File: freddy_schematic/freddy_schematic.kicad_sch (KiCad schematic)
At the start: 2 parts, among them U1 ESP32-C3-DevKitC-02

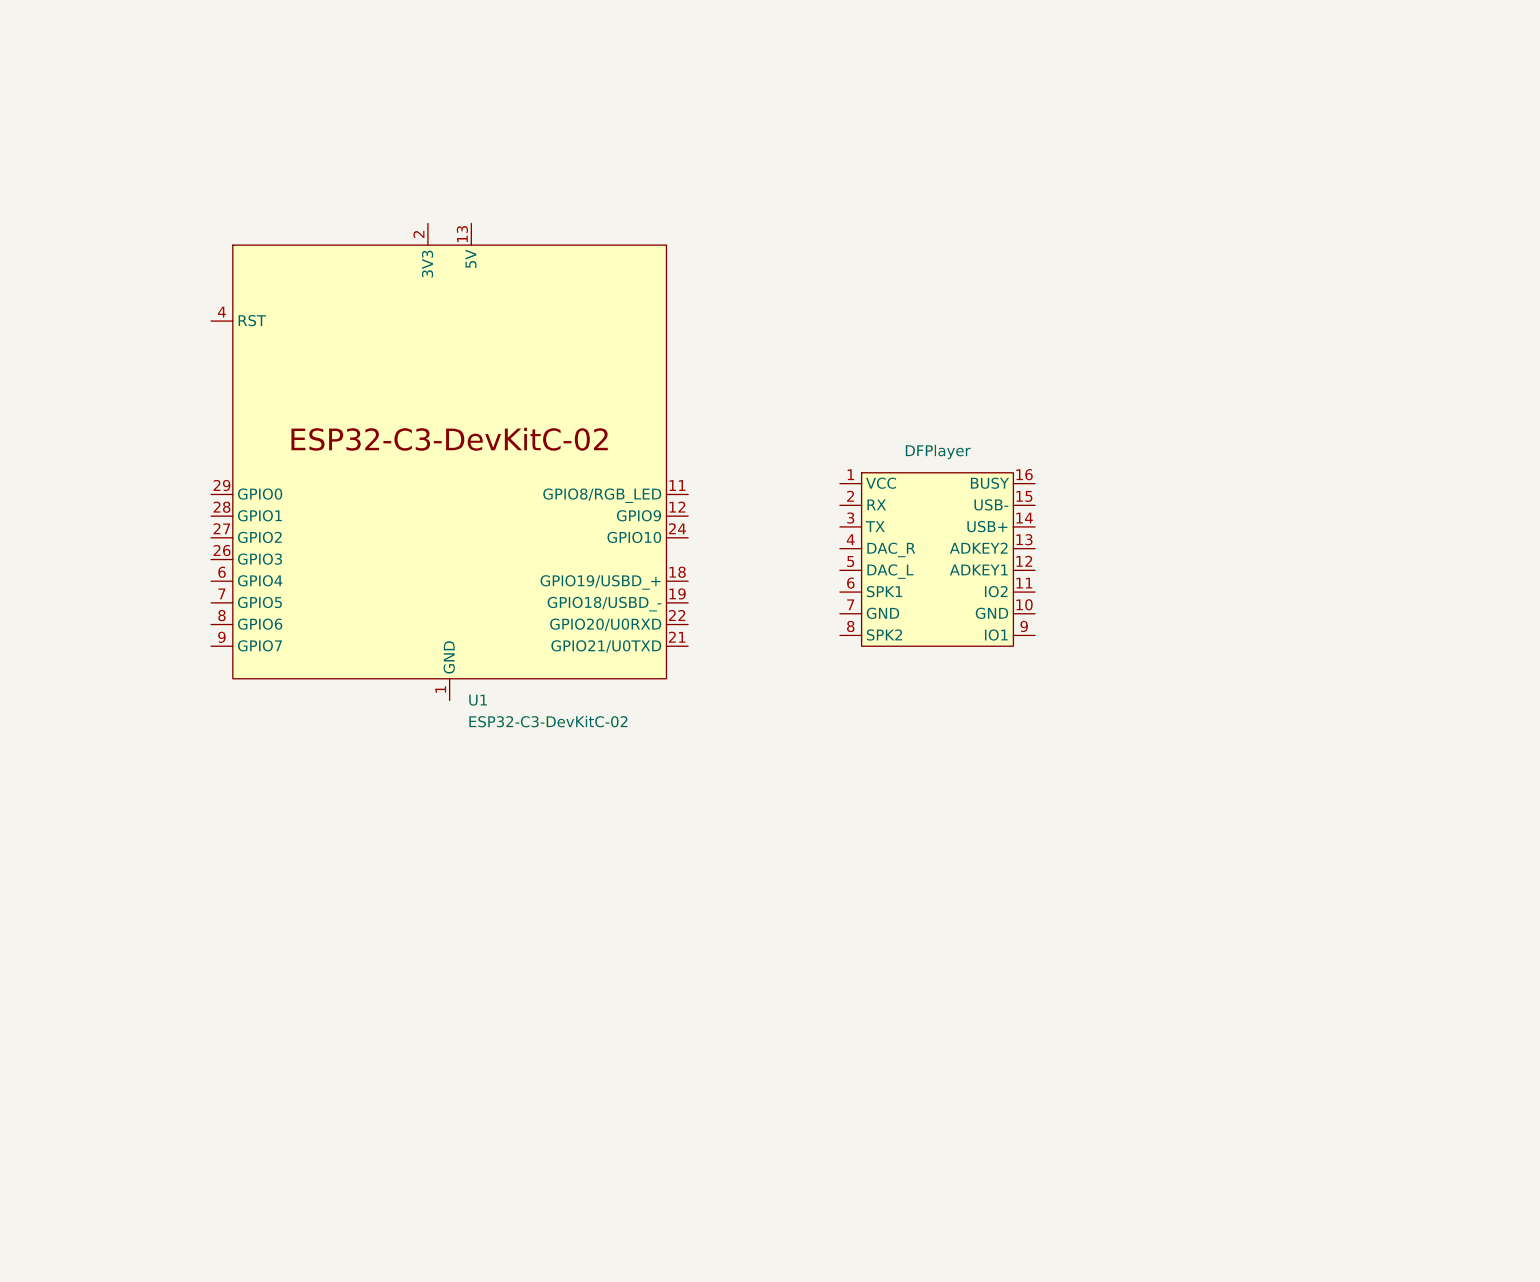
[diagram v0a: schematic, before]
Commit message: complete schematic
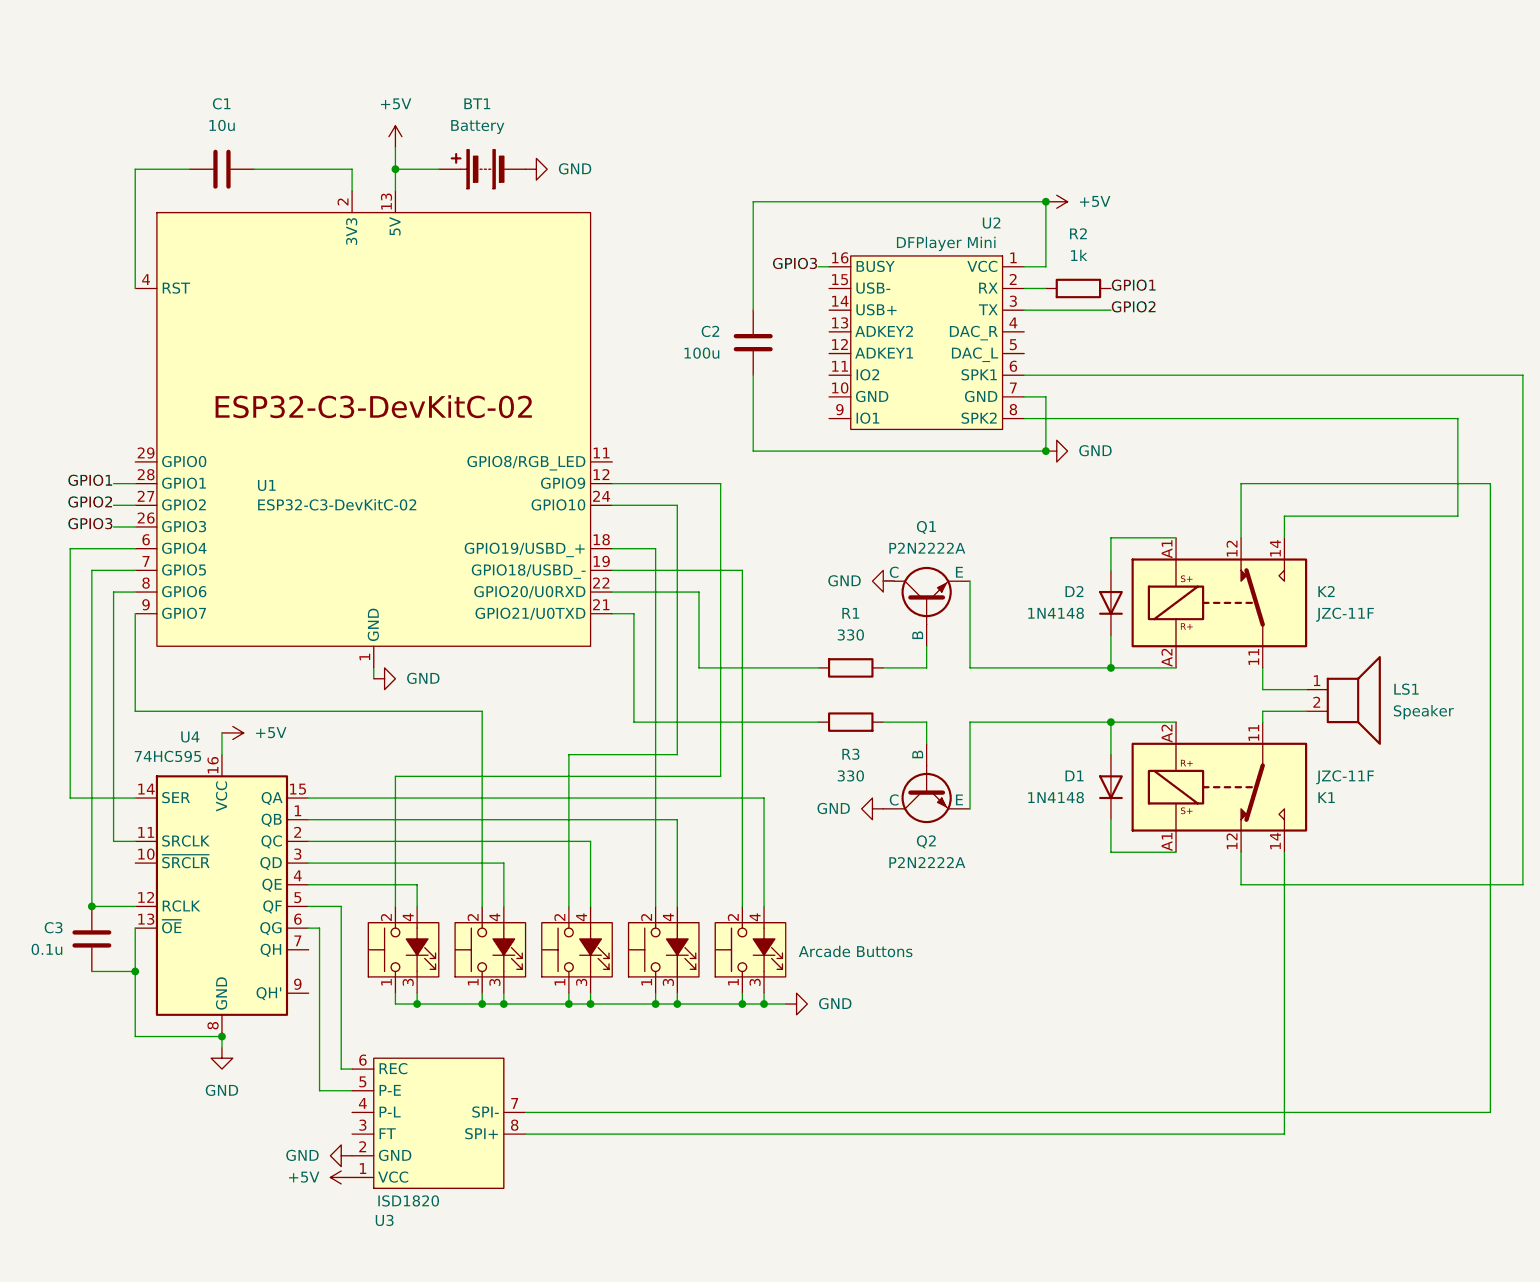
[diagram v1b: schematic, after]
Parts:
- removed DFPlayer: (no value), symbol PCB_periperals:DFPlayer_Mini
- added BT1: Battery, symbol Device:Battery
- added C1: 10u, symbol Device:C
- added C2: 100u, symbol Device:C
- added C3: 0.1u, symbol Device:C
- added D1, D2: 1N4148, Diode_THT:D_DO-35_SOD27_P7.62mm_Horizontal, symbol Diode:1N4148
- added K1, K2: JZC-11F, symbol Relay:Relay_SPDT_Latching_1coil
- added LS1: Speaker, symbol Device:Speaker
- added Q1, Q2: P2N2222A, symbol Simulation_SPICE:NPN
- added R1, R3: 330, symbol Device:R
- added R2: 1k, symbol Device:R
- added SW1: Arcade Buttons, symbol Switch:SW_Push_LED
- added SW2, SW3, SW4, SW5: Arcade Button, symbol Switch:SW_Push_LED
- added U2: DFPlayer Mini, symbol PCB_periperals:DFPlayer_Mini
- added U3: ISD1820, symbol PCB_periperals:ISD1820
- added U4: 74HC595, symbol 74xx:74HC595
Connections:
- net 3V3: now also C1.2
- net GND: now reaches U1.1 (GND), U1.10 (GND), U1.15 (GND), U1.16 (GND), U1.17 (GND), U1.20 (GND), U1.23 (GND), U1.25 (GND), U1.30 (GND), U1.5 (GND)
- net GND: now also BT1.2 (-), C2.2, C3.1, Q1.1 (C), Q2.1 (C), SW1.1, SW1.3 (K), SW2.1, SW2.3 (K), SW3.1, SW3.3 (K), SW4.1, SW4.3 (K), SW5.1, SW5.3 (K), U2.7 (GND), U3.2 (GND), U4.13 (~{OE}), U4.8 (GND)
- net at U1.12 (GPIO9): now also SW1.2
- net at U1.18 (GPIO19/USBD_+): now also SW4.2
- net at U1.19 (GPIO18/USBD_-): now also SW5.2
- net at U1.21 (GPIO21/U0TXD): now also R3.1
- net at U1.22 (GPIO20/U0RXD): now also R1.2
- net at U1.24 (GPIO10): now also SW3.2
- net GPIO3: now reaches U1.26 (GPIO3)
- net GPIO3: now also U2.16 (BUSY)
- net GPIO2: now reaches U1.27 (GPIO2)
- net GPIO2: now also U2.3 (TX)
- net GPIO1: now reaches U1.28 (GPIO1)
- net GPIO1: now also R2.1
- net at U1.4 (RST): now also C1.1
- net at U1.6 (GPIO4): now also U4.14 (SER)
- net at U1.7 (GPIO5): now also C3.2, U4.12 (RCLK)
- net at U1.8 (GPIO6): now also U4.11 (SRCLK)
- net at U1.9 (GPIO7): now also SW2.2
- net 5V renamed +5V
- net +5V: now also BT1.1 (+), C2.1, U2.1 (VCC), U3.1 (VCC), U4.16 (VCC)
- new net: R2.2, U2.2 (RX)
- new net: K1.12, U2.6 (SPK1)
- new net: K2.14, U2.8 (SPK2)
- new net: Q2.2 (B), R3.2
- new net: D1.2 (A), K1.A2, Q2.3 (E)
- new net: K2.11, LS1.1
- new net: K2.12, U3.7 (SPI-)
- new net: D2.2 (A), K2.A1
- new net: D2.1 (K), K2.A2, Q1.3 (E)
- new net: SW1.4 (A), U4.4 (QE)
- new net: K1.11, LS1.2
- new net: D1.1 (K), K1.A1
- new net: U3.5 (P-E), U4.6 (QG)
- new net: U3.6 (REC), U4.5 (QF)
- new net: K1.14, U3.8 (SPI+)
- new net: SW4.4 (A), U4.1 (QB)
- new net: SW2.4 (A), U4.3 (QD)
- new net: SW5.4 (A), U4.15 (QA)
- new net: SW3.4 (A), U4.2 (QC)
- new net: Q1.2 (B), R1.1

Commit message: fixed schematic
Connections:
- net +5V: now also U4.10 (~{SRCLR})
- net 3V3: no longer C1.2
- net GND: now also C1.1
- net at U1.4 (RST): now also C1.2; no longer C1.1
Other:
- moved on the sheet: C1
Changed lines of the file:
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@@
 	(wire
 		(pts
-			(xy 128.27 105.41) (xy 115.57 105.41)
+			(xy 57.15 53.34) (xy 57.15 50.8)
 		)
 		(stroke
@@
 	(wire
 		(pts
-			(xy 125.73 133.35) (xy 125.73 134.62)
+			(xy 128.27 105.41) (xy 115.57 105.41)
 		)
 		(stroke
@@
 	(wire
 		(pts
-			(xy 85.09 120.65) (xy 97.79 120.65)
+			(xy 125.73 133.35) (xy 125.73 134.62)
 		)
 		(stroke
@@
 	(wire
 		(pts
-			(xy 97.79 134.62) (xy 105.41 134.62)
+			(xy 85.09 120.65) (xy 97.79 120.65)
 		)
 		(stroke
@@
 	(wire
 		(pts
-			(xy 138.43 110.49) (xy 138.43 123.19)
+			(xy 97.79 134.62) (xy 105.41 134.62)
 		)
 		(stroke
@@
 	(wire
 		(pts
-			(xy 74.93 138.43) (xy 64.77 138.43)
+			(xy 138.43 110.49) (xy 138.43 123.19)
 		)
 		(stroke
@@
 	(wire
 		(pts
-			(xy 57.15 81.28) (xy 57.15 110.49)
+			(xy 74.93 138.43) (xy 64.77 138.43)
 		)
 		(stroke
@@
 	(wire
 		(pts
-			(xy 71.12 36.83) (xy 64.77 36.83)
+			(xy 57.15 81.28) (xy 57.15 110.49)
 		)
 		(stroke
@@
 	(wire
 		(pts
-			(xy 78.74 36.83) (xy 90.17 36.83)
-		)
-		(stroke
-			(width 0)
-			(type default)
-		)
-	)
-	(wire
-		(pts
 			(xy 179.07 101.6) (xy 179.07 105.41)
 		)
@@
 	(wire
 		(pts
-			(xy 90.17 36.83) (xy 90.17 39.37)
-		)
-		(stroke
-			(width 0)
-			(type default)
-		)
-	)
-	(wire
-		(pts
 			(xy 120.65 86.36) (xy 130.81 86.36)
 		)
@@
 	(wire
 		(pts
-			(xy 64.77 36.83) (xy 64.77 50.8)
-		)
-		(stroke
-			(width 0)
-			(type default)
-		)
-	)
-	(wire
-		(pts
 			(xy 88.9 142.24) (xy 88.9 123.19)
 		)
@@
 	(symbol
 		(lib_id "Device:C")
-		(at 74.93 36.83 90)
+		(at 60.96 50.8 90)
 		(unit 1)
 		(body_style 1)
@@
 		(fields_autoplaced yes)
 		(property "Reference" "C1"
-			(at 74.93 29.21 90)
+			(at 60.96 43.18 90)
 			(show_name no)
 			(do_not_autoplace no)
@@
 		)
 		(property "Value" "10u"
-			(at 74.93 31.75 90)
+			(at 60.96 45.72 90)
 			(show_name no)
 			(do_not_autoplace no)
@@
 		)
 		(property "Footprint" ""
-			(at 78.74 35.8648 0)
+			(at 64.77 49.8348 0)
 			(hide yes)
 			(show_name no)
@@
 		)
 		(property "Datasheet" ""
-			(at 74.93 36.83 0)
+			(at 60.96 50.8 0)
 			(hide yes)
 			(show_name no)
@@
 		)
 		(property "Description" "Unpolarized capacitor"
-			(at 74.93 36.83 0)
+			(at 60.96 50.8 0)
 			(hide yes)
 			(show_name no)
@@
 	(symbol
 		(lib_id "power:GND")
+		(at 57.15 53.34 0)
+		(unit 1)
+		(body_style 1)
+		(exclude_from_sim no)
+		(in_bom yes)
+		(on_board yes)
+		(in_pos_files yes)
+		(dnp no)
+		(fields_autoplaced yes)
+		(property "Reference" "#PWR03"
+			(at 57.15 59.69 0)
+			(hide yes)
+			(show_name no)
+			(do_not_autoplace no)
+			(effects
+				(font
+					(size 1.27 1.27)
+				)
+			)
+		)
+		(property "Value" "GND"
+			(at 57.15 58.42 0)
+			(show_name no)
+			(do_not_autoplace no)
+			(effects
+				(font
+					(size 1.27 1.27)
+				)
+			)
+		)
+		(property "Footprint" ""
+			(at 57.15 53.34 0)
+			(hide yes)
+			(show_name no)
+			(do_not_autoplace no)
+			(effects
+				(font
+					(size 1.27 1.27)
+				)
+			)
+		)
+		(property "Datasheet" ""
+			(at 57.15 53.34 0)
+			(hide yes)
+			(show_name no)
+			(do_not_autoplace no)
+			(effects
+				(font
+					(size 1.27 1.27)
+				)
+			)
+		)
+		(property "Description" "Power symbol creates a global label with name \"GND\" , ground"
+			(at 57.15 53.34 0)
+			(hide yes)
+			(show_name no)
+			(do_not_autoplace no)
+			(effects
+				(font
+					(size 1.27 1.27)
+				)
+			)
+		)
+		(pin "1"
+		)
+		(instances
+			(project "freddy_schematic"
+				(path "/1b5976a3-0692-47b4-aad3-0176734612a9"
+					(reference "#PWR03")
+					(unit 1)
+				)
+			)
+		)
+	)
+	(symbol
+		(lib_id "power:GND")
 		(at 152.4 111.76 270)
 		(unit 1)
@@
 					(unit 1)
 				)
+			)
+		)
+	)
+	(symbol
+		(lib_id "power:+5V")
+		(at 64.77 118.11 90)
+		(unit 1)
+		(body_style 1)
+		(exclude_from_sim no)
+		(in_bom yes)
+		(on_board yes)
+		(in_pos_files yes)
+		(dnp no)
+		(property "Reference" "#PWR014"
+			(at 68.58 118.11 0)
+			(hide yes)
+			(show_name no)
+			(do_not_autoplace no)
+			(effects
+				(font
+					(size 1.27 1.27)
+				)
+			)
+		)
+		(property "Value" "+5V"
+			(at 64.77 120.142 90)
+			(show_name no)
+			(do_not_autoplace no)
+			(effects
+				(font
+					(size 1.27 1.27)
+				)
+				(justify left)
+			)
+		)
+		(property "Footprint" ""
+			(at 64.77 118.11 0)
+			(hide yes)
+			(show_name no)
+			(do_not_autoplace no)
+			(effects
+				(font
+					(size 1.27 1.27)
+				)
+			)
+		)
+		(property "Datasheet" ""
+			(at 64.77 118.11 0)
+			(hide yes)
+			(show_name no)
+			(do_not_autoplace no)
+			(effects
+				(font
+					(size 1.27 1.27)
+				)
+			)
+		)
+		(property "Description" "Power symbol creates a global label with name \"+5V\""
+			(at 64.77 118.11 0)
+			(hide yes)
+			(show_name no)
+			(do_not_autoplace no)
+			(effects
+				(font
+					(size 1.27 1.27)
+				)
+			)
+		)
+		(pin "1"
+		)
+		(instances
+			(project "freddy_schematic"
+				(path "/1b5976a3-0692-47b4-aad3-0176734612a9"
+					(reference "#PWR014")
+					(unit 1)
+				)
